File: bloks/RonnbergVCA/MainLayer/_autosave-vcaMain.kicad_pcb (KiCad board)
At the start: 2 copper layers, 91.4 x 45.7 mm, 38 parts, among them J1 Conn_02x03_Odd_Even, J10 Conn_02x03_Odd_Even, J11 Conn_02x03_Odd_Even, J12 Conn_02x03_Odd_Even, J1M1 Conn_01x01, J2 Conn_02x03_Odd_Even, J2M1 Conn_01x01, J3 Conn_02x03_Odd_Even, J3M1 Conn_01x01, J4 Conn_02x03_Odd_Even, J4M1 Conn_01x01, J5 Conn_02x03_Odd_Even, J5M1 Conn_01x01, J6 Conn_02x03_Odd_Even, J6M1 Conn_01x01, J7 Conn_02x03_Odd_Even, J7M1 Conn_01x01, J8 Conn_02x03_Odd_Even, J9 Conn_02x03_Odd_Even, U1 TL072, U2 CA3080

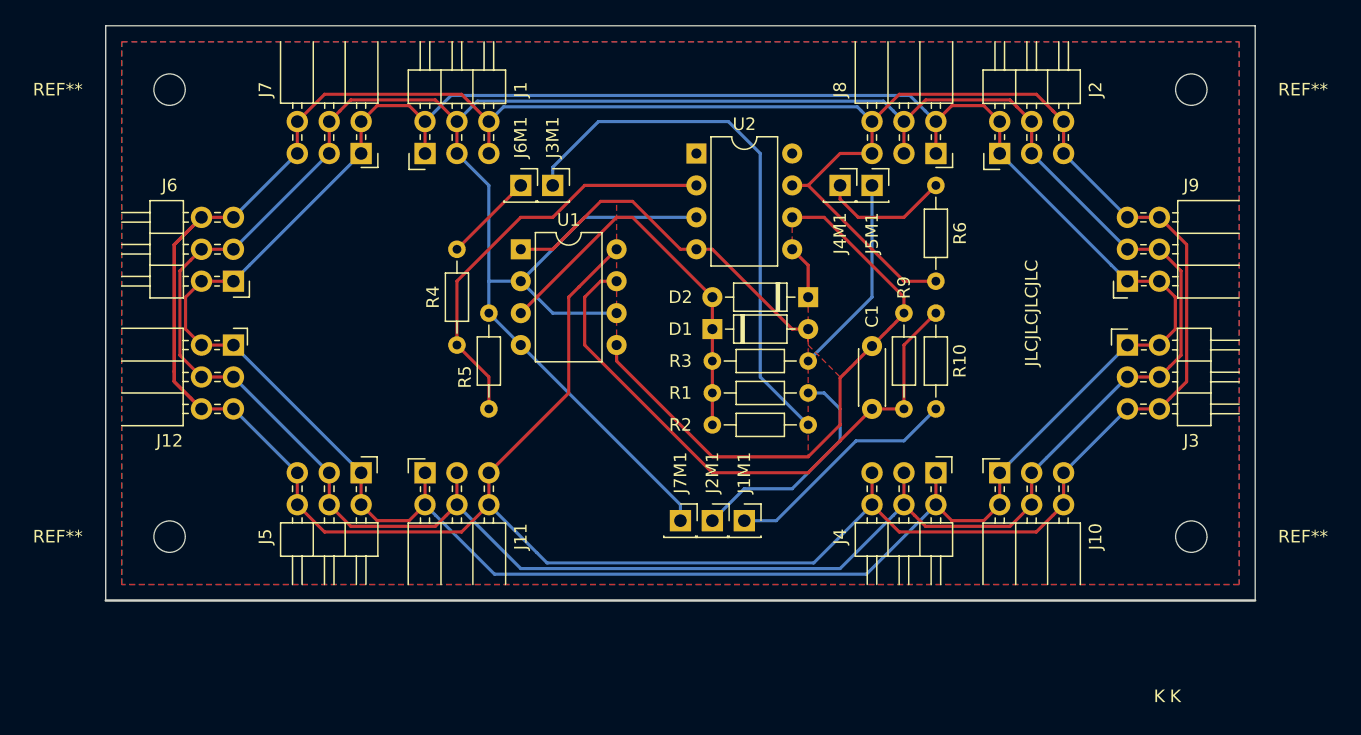
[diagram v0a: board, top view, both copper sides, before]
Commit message: Added -12v rail to power headers
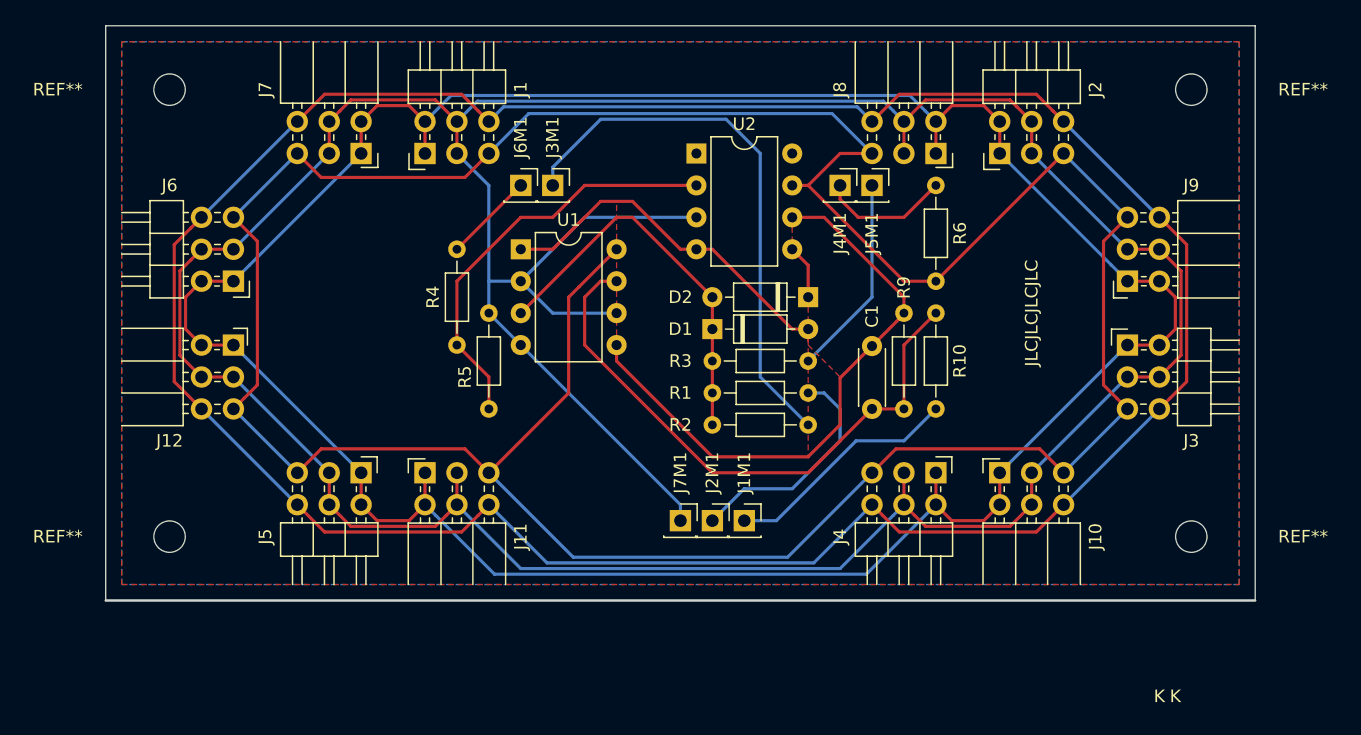
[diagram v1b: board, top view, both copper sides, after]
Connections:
- J1 pad 6: +12V -> -12V
- J10 pad 6: +12V -> -12V
- J11 pad 6: +12V -> -12V
- J12 pad 6: +12V -> -12V
- J2 pad 6: +12V -> -12V
- J3 pad 6: +12V -> -12V
- J4 pad 6: +12V -> -12V
- J5 pad 6: +12V -> -12V
- J6 pad 6: +12V -> -12V
- J7 pad 6: +12V -> -12V
- J8 pad 6: +12V -> -12V
- J9 pad 6: +12V -> -12V
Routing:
- net -12V: track 0.00 -> 211.1 mm
- net +12V: track 287.0 -> 239.1 mm
